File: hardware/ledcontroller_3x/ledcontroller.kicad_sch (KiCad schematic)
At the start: 88 parts, among them J1 ADC, J10 GPIO10, J11 MOSI, J12 SCLK, J13 TX, J14 RX, J15 FLASH, J16 SCL, J17 SDA, J18 OE, J19 Pololu D24V5F3, J2 GPIO16, J20 VIN, J21 GND, J22 24V, J23 RED, J24 GREEN, J25 BLUE, J26 W_WHITE, J27 C_WHITE, J28 24V, J29 RED, J3 GPIO14, J30 GREEN, J31 BLUE, J32 W_WHITE, J33 C_WHITE, J34 24V, J35 RED, J36 GREEN, J37 BLUE, J38 W_WHITE, J39 C_WHITE, J4 GPIO12, J5 GPIO13, J6 RESET, J7 CS0, J8 MISO, J9 GPIO9, Q1 BLM3400, Q10 BLM3400, Q11 BLM3400, Q12 BLM3400, Q13 BLM3400, Q14 BLM3400, Q15 BLM3400, Q2 BLM3400, Q3 BLM3400, Q4 BLM3400, Q5 BLM3400, Q6 BLM3400, Q7 BLM3400, Q8 BLM3400, Q9 BLM3400, U1 ESP-12E, U2 PCA9685PW

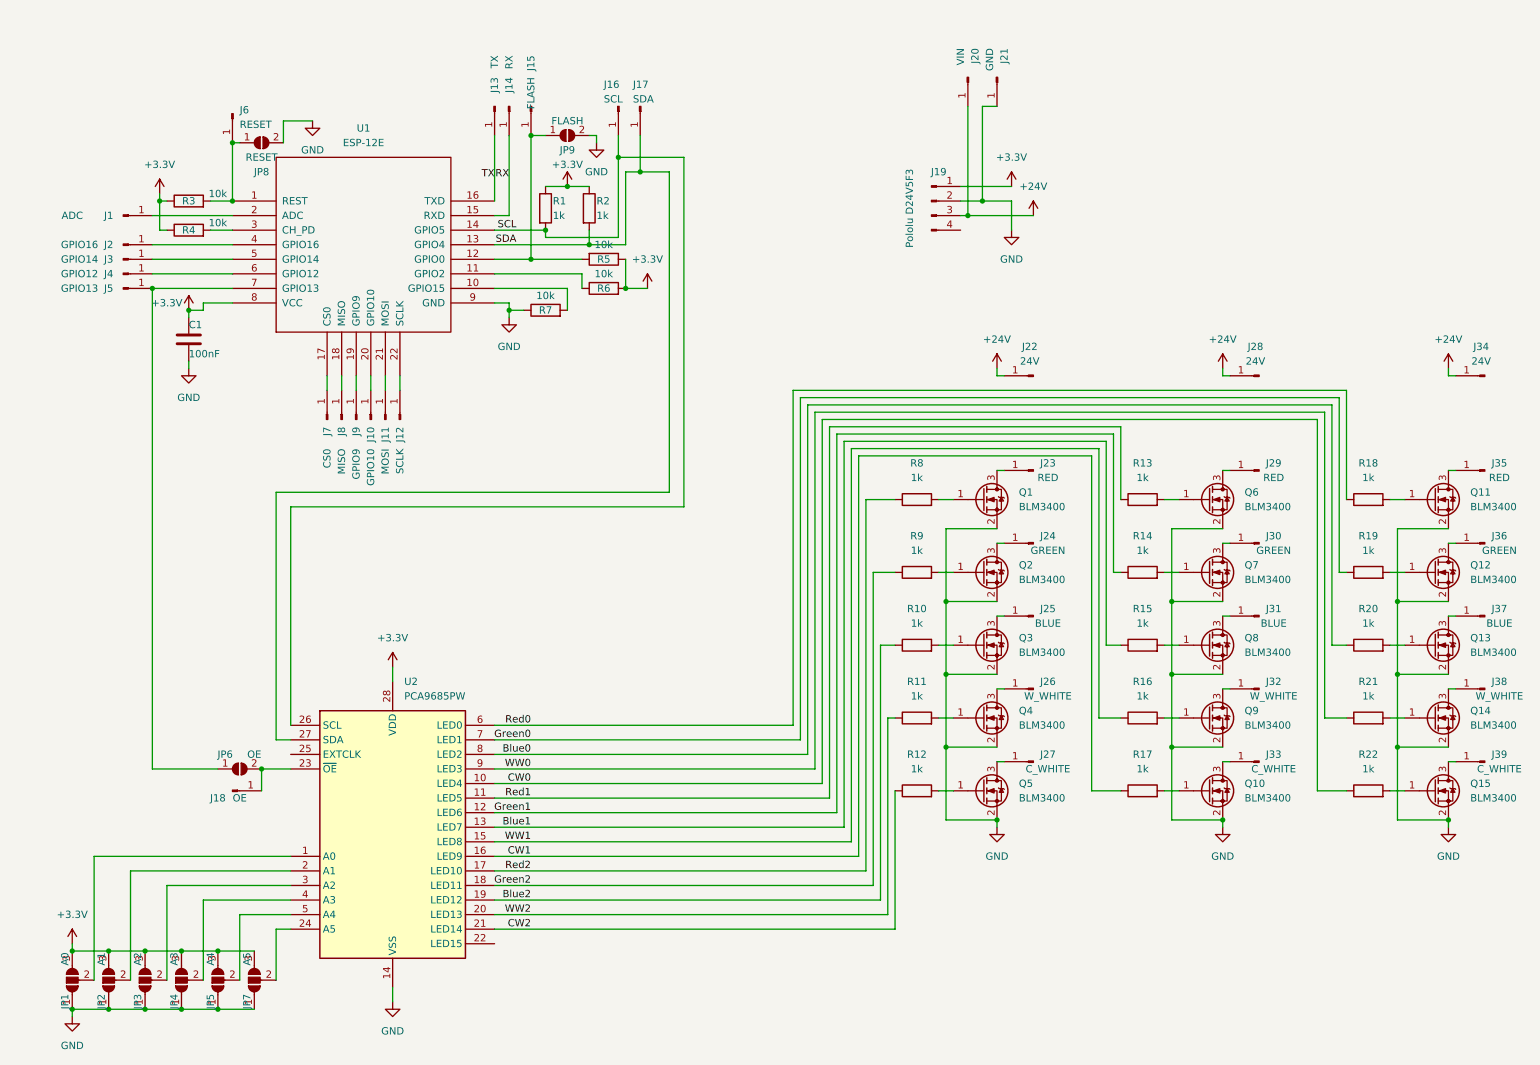
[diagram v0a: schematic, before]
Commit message: Updated PCB to combat flickering with higher current LEDs or longer strips
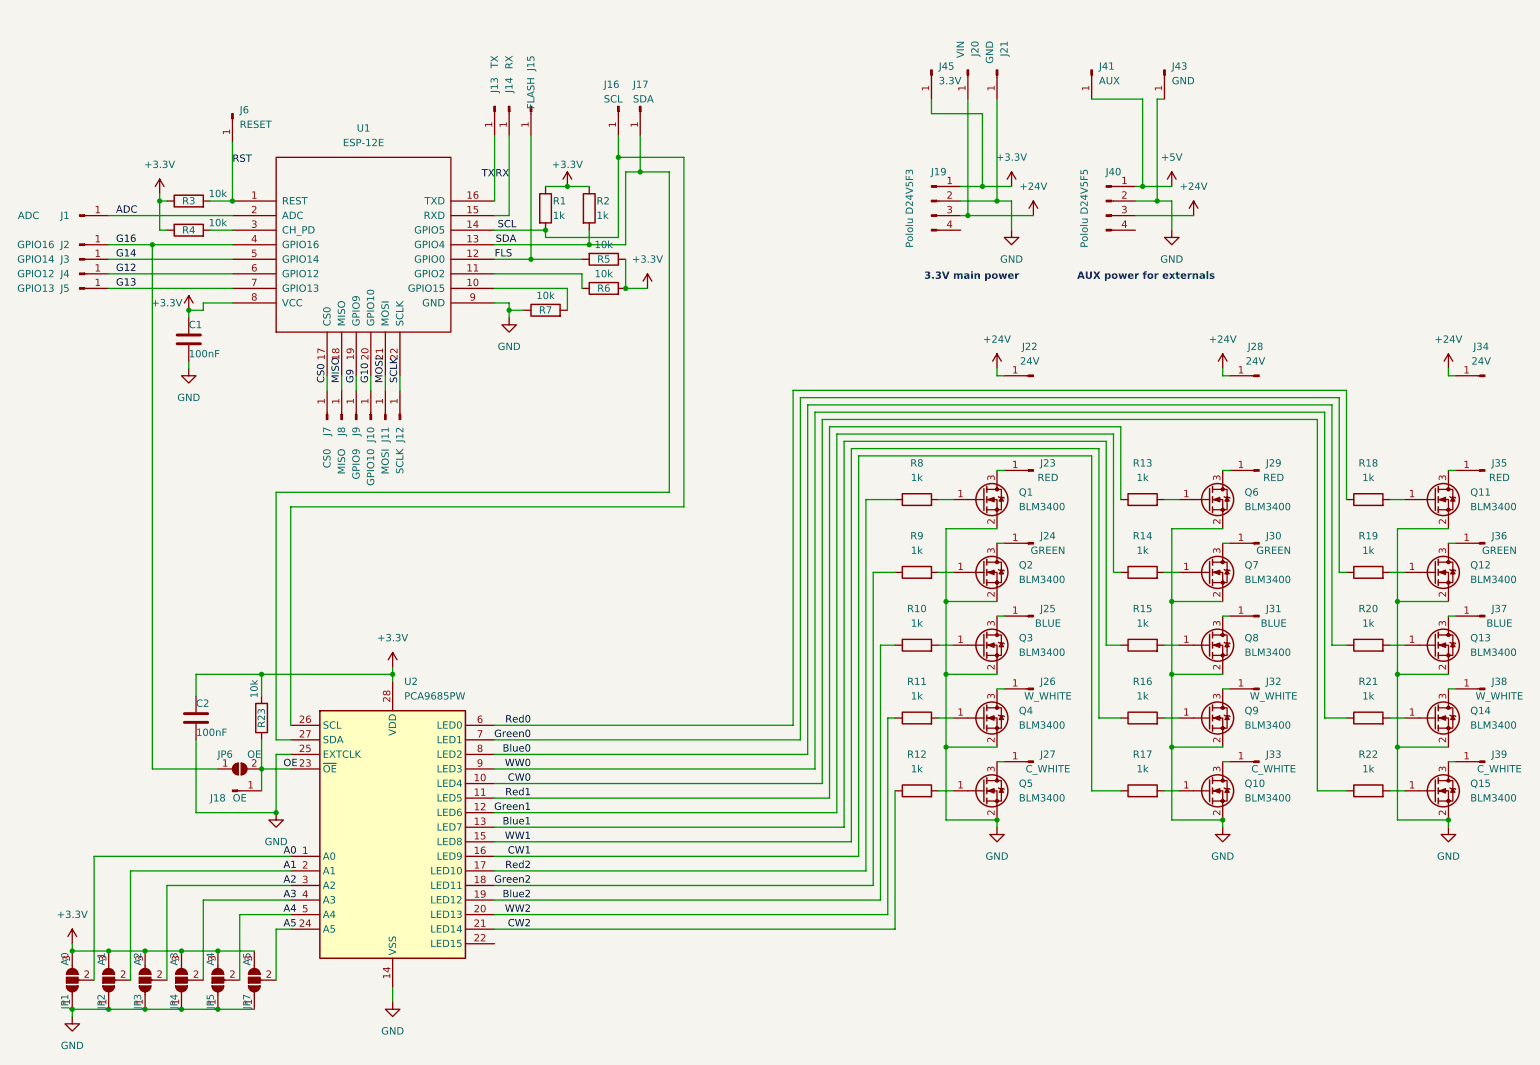
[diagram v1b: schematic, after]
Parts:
- removed JP8: RESET, Jumper:SolderJumper-2_P1.3mm_Open_Pad1.0x1.5mm, symbol Jumper:SolderJumper_2_Open
- removed JP9: FLASH, Jumper:SolderJumper-2_P1.3mm_Open_Pad1.0x1.5mm, symbol Jumper:SolderJumper_2_Open
- added C2: 100nF, Capacitor_SMD:C_0805_2012Metric, symbol Device:C
- added J40: Pololu D24V5F5, Connector_PinHeader_2.54mm:PinHeader_1x04_P2.54mm_Vertical, symbol Connector:Conn_01x04_Male
- added J41: AUX, TestPoint:TestPoint_Pad_3.0x3.0mm, symbol Connector:Conn_01x01_Male
- added J43: GND, TestPoint:TestPoint_Pad_3.0x3.0mm, symbol Connector:Conn_01x01_Male
- added J45: 3.3V, TestPoint:TestPoint_Pad_3.0x3.0mm, symbol Connector:Conn_01x01_Male
- added R23: 10k, Resistor_SMD:R_0805_2012Metric, symbol Device:R
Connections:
- net +24V: now also J40.3 (Pin_3)
- net +3.3V: now also C2.1, J45.1 (Pin_1), R23.2
- net GND: now also U2.25 (EXTCLK), C2.2, J40.2 (Pin_2), J43.1 (Pin_1)
- net ADC: now reaches J1.1 (Pin_1), U1.2 (ADC)
- net A0: now reaches JP1.2 (C), U2.1 (A0)
- net A1: now reaches JP2.2 (C), U2.2 (A1)
- net OE: now reaches J18.1 (Pin_1), JP6.2 (B), U2.23 (~{OE})
- net OE: now also R23.1
- net A5: now reaches JP7.2 (C), U2.24 (A5)
- net A2: now reaches JP3.2 (C), U2.3 (A2)
- net A3: now reaches JP4.2 (C), U2.4 (A3)
- net A4: now reaches JP5.2 (C), U2.5 (A4)
- net RST: now reaches J6.1 (Pin_1), R3.2, U1.1 (REST)
- net SCLK: now reaches J12.1 (Pin_1), U1.22 (SCLK)
- net G13: now reaches J5.1 (Pin_1), U1.7 (GPIO13)
- net G13: no longer JP6.1 (A)
- net MISO: now reaches J8.1 (Pin_1), U1.18 (MISO)
- net FLS: now reaches J15.1 (Pin_1), R5.2, U1.12 (GPIO0)
- net CS0: now reaches J7.1 (Pin_1), U1.17 (CS0)
- net G9: now reaches J9.1 (Pin_1), U1.19 (GPIO9)
- net G10: now reaches J10.1 (Pin_1), U1.20 (GPIO10)
- net MOSI: now reaches J11.1 (Pin_1), U1.21 (MOSI)
- net G16: now reaches J2.1 (Pin_1), U1.4 (GPIO16)
- net G16: now also JP6.1 (A)
- net G14: now reaches J3.1 (Pin_1), U1.5 (GPIO14)
- net G12: now reaches J4.1 (Pin_1), U1.6 (GPIO12)
- new net +5V: J40.1 (Pin_1), J41.1 (Pin_1)
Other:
- note added: "3.3V main power"
- note added: "AUX power for externals"
- moved on the sheet: J1, J2, J20, J21, J3, J4, J5

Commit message: Updated PCB: additional decoupling capacitors, switchable I2C pullups, made OE pulled down instead of pulled up
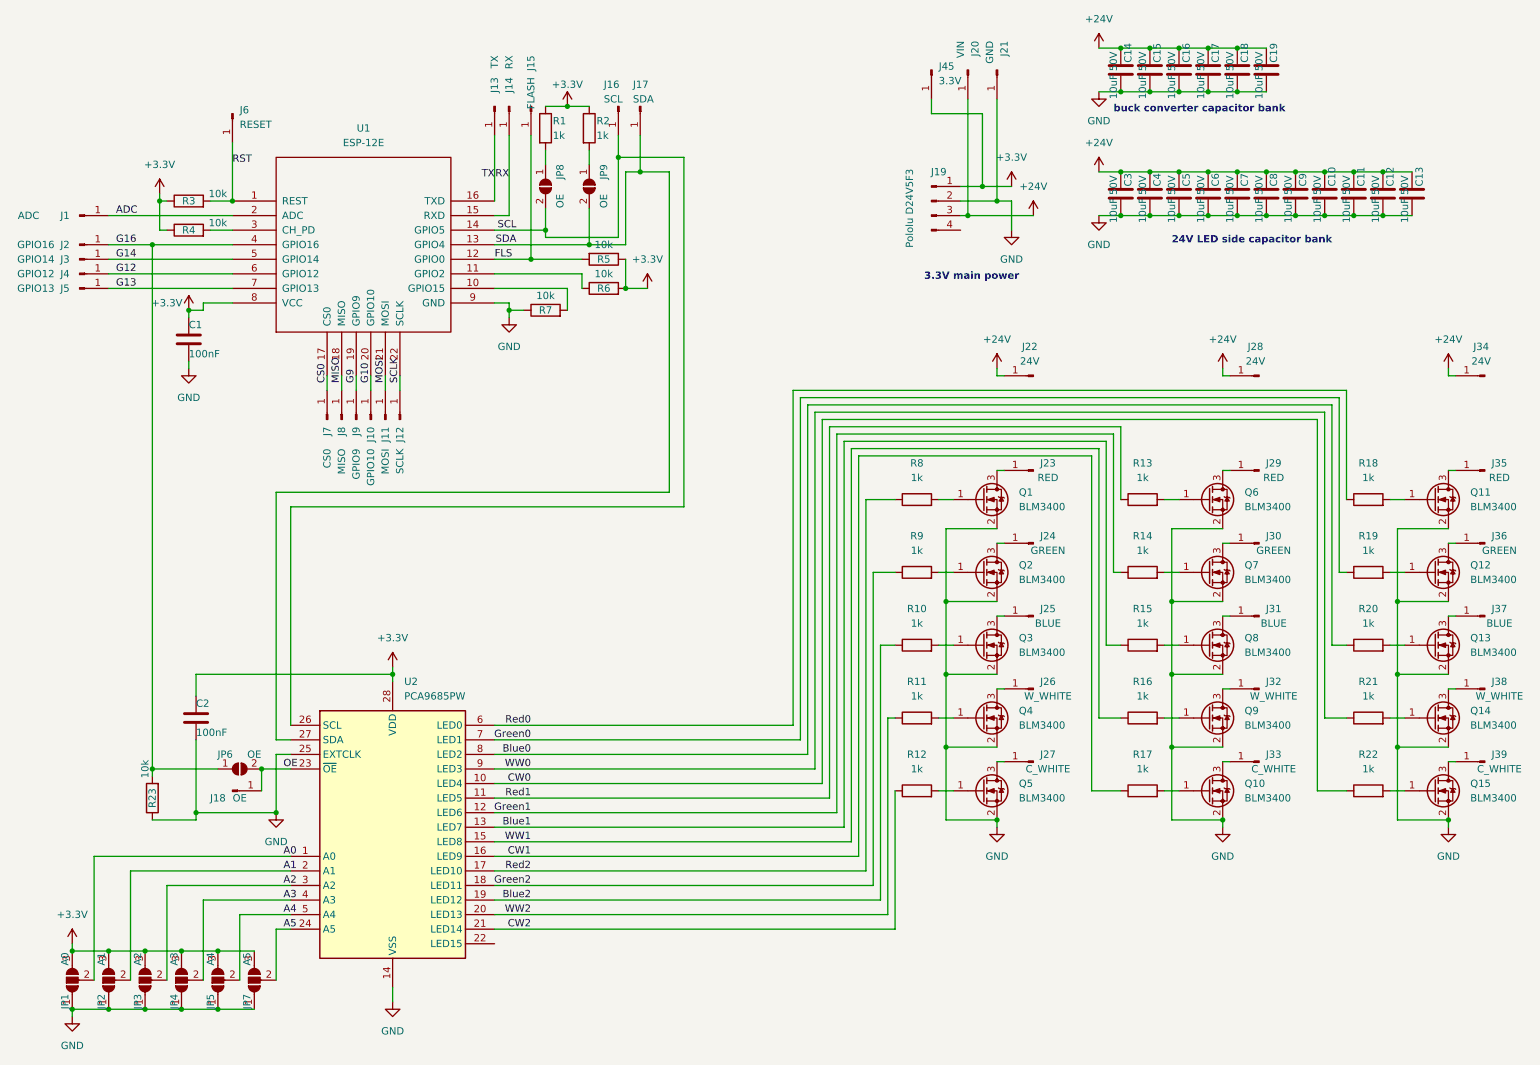
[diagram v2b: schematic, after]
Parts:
- removed J40: Pololu D24V5F5, Connector_PinHeader_2.54mm:PinHeader_1x04_P2.54mm_Vertical, symbol Connector:Conn_01x04_Male
- removed J41: AUX, TestPoint:TestPoint_Pad_3.0x3.0mm, symbol Connector:Conn_01x01_Male
- removed J43: GND, TestPoint:TestPoint_Pad_3.0x3.0mm, symbol Connector:Conn_01x01_Male
- added C10, C11, C12, C13, C14, C15, C16, C17, C18, C19, C3, C4, C5, C6, C7, C8, C9: 10uF 50V, Capacitor_SMD:C_0805_2012Metric, symbol Device:C
- added JP8, JP9: OE, Jumper:SolderJumper-2_P1.3mm_Open_Pad1.0x1.5mm, symbol Jumper:SolderJumper_2_Open
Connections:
- net +24V: now also C10.1, C11.1, C12.1, C13.1, C14.1, C15.1, C16.1, C17.1, C18.1, C19.1, C3.1, C4.1, C5.1, C6.1, C7.1, C8.1, C9.1
- net +3.3V: no longer R23.2
- net G16: now also R23.2
- net GND: now also R23.1, C10.2, C11.2, C12.2, C13.2, C14.2, C15.2, C16.2, C17.2, C18.2, C19.2, C3.2, C4.2, C5.2, C6.2, C7.2, C8.2, C9.2
- net OE: no longer R23.1
- net SCL: now also JP8.2 (B); no longer R1.2
- net SDA: now also JP9.2 (B); no longer R2.2
- new net: JP8.1 (A), R1.2
- new net: JP9.1 (A), R2.2
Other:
- note added: "24V LED side capacitor bank"
- note added: "buck converter capacitor bank"
- note removed: "AUX power for externals"
- moved on the sheet: R1, R2, R23

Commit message: replaced ceramic capacitors with low ESR electrolytic caps
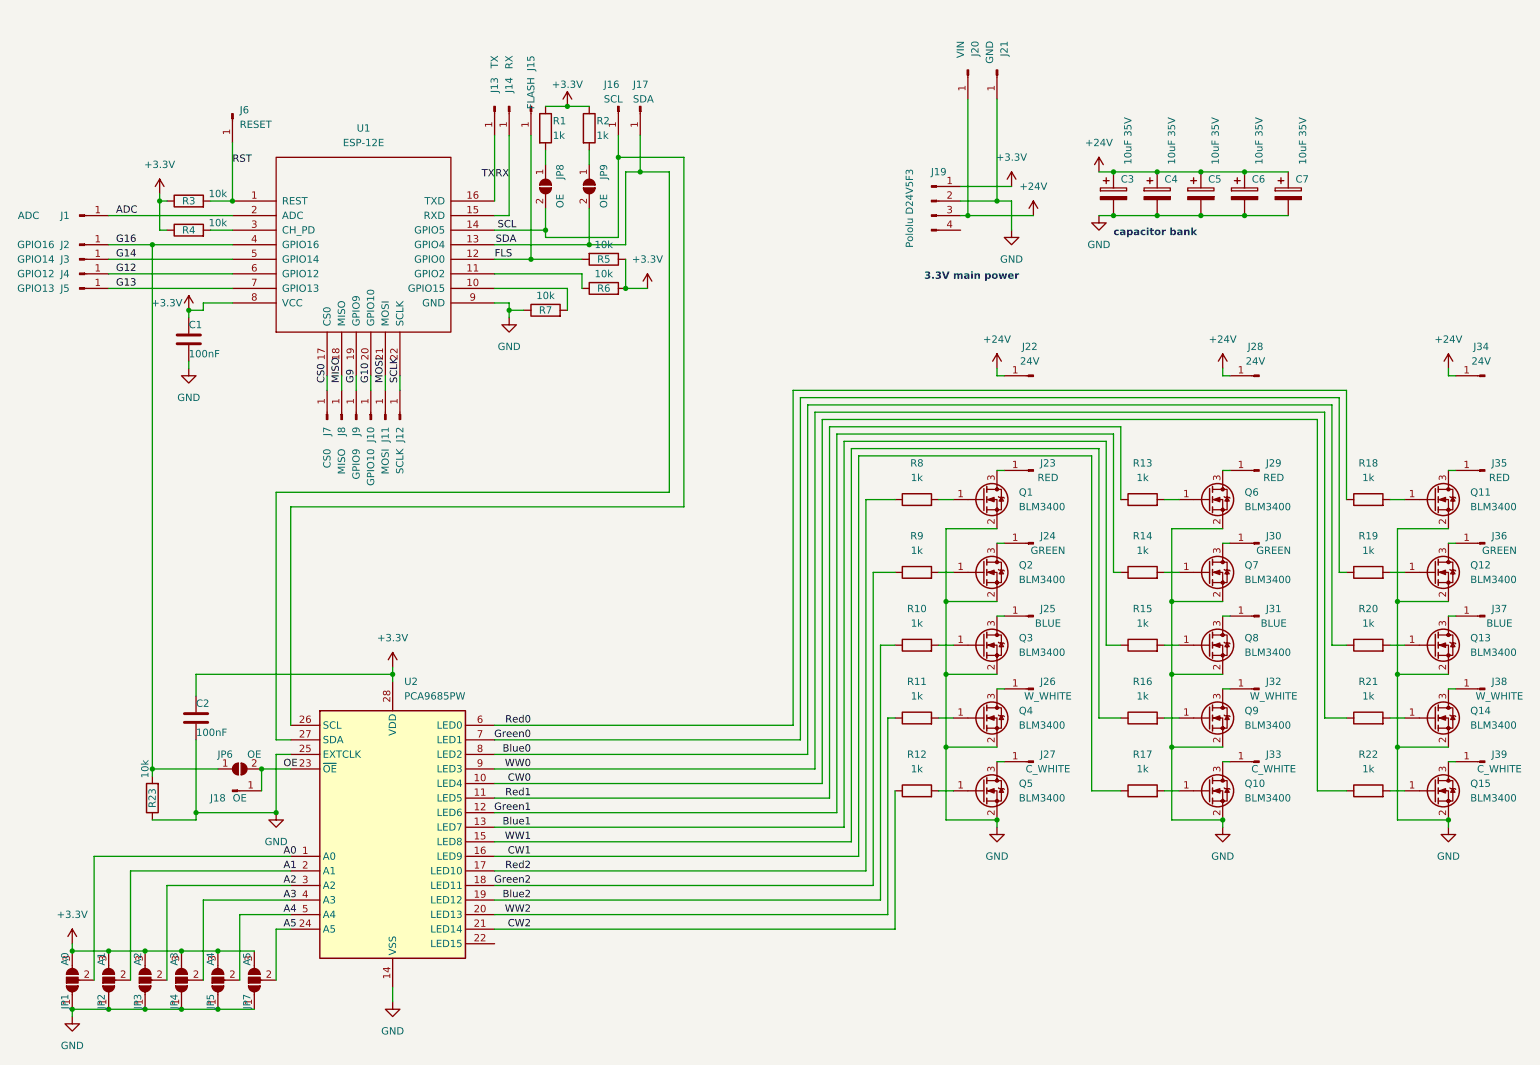
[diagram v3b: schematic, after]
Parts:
- removed C10, C11, C12, C13, C14, C15, C16, C17, C18, C19, C3, C4, C5, C6, C7, C8, C9: 10uF 50V, Capacitor_SMD:C_0805_2012Metric, symbol Device:C
- removed J45: 3.3V, TestPoint:TestPoint_Pad_3.0x3.0mm, symbol Connector:Conn_01x01_Male
- added C3, C4, C5, C6, C7: 10uF 35V, Capacitor_SMD:CP_Elec_5x5.4, symbol Device:C_Polarized
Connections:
- net +24V: now also C3.1, C4.1, C5.1, C6.1, C7.1
- net GND: now also C3.2, C4.2, C5.2, C6.2, C7.2
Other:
- note added: "capacitor bank"
- note removed: "24V LED side capacitor bank"
- note removed: "buck converter capacitor bank"

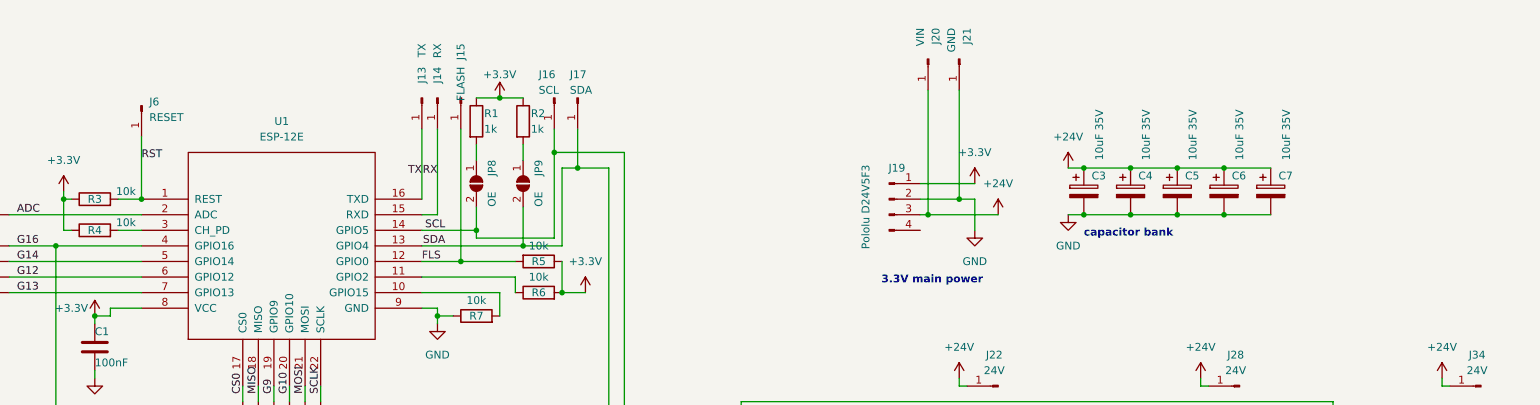
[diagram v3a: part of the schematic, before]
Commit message: added autoprogram circuit to schematic
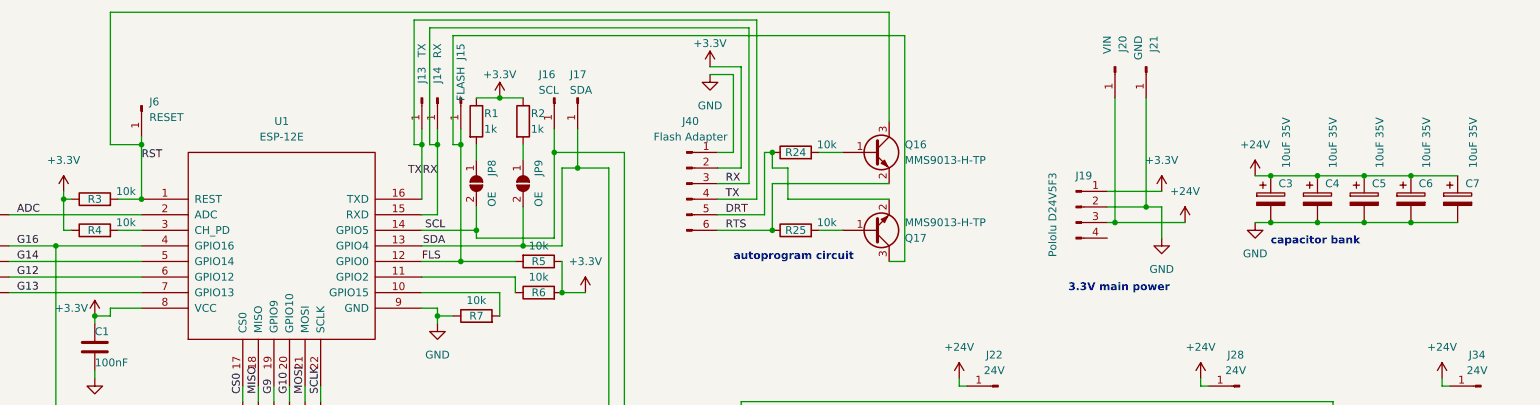
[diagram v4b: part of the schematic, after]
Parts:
- added J40: Flash Adapter, symbol Connector:Conn_01x06_Pin
- added Q16, Q17: MMS9013-H-TP, Package_TO_SOT_SMD:SOT-23, symbol Transistor_BJT:BC817
- added R24, R25: 10k, Resistor_SMD:R_0805_2012Metric, symbol Device:R
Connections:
- net +3.3V: now also J40.2 (Pin_2)
- net FLS: now also Q17.3 (C)
- net GND: now also J40.1 (Pin_1)
- net RST: now also Q16.3 (C)
- net RX: now also J40.3 (Pin_3)
- net TX: now also J40.4 (Pin_4)
- new net: Q17.1 (B), R25.2
- new net: Q16.1 (B), R24.2
- new net DRT: J40.5 (Pin_5), Q17.2 (E), R24.1
- new net RTS: J40.6 (Pin_6), Q16.2 (E), R25.1
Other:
- note added: "autoprogram circuit"
- moved on the sheet: C3, C4, C5, C6, C7, J19, J20, J21
